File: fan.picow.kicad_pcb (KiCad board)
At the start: 2 copper layers, 73.4 x 70.5 mm, 64 parts, among them J1 12v Input, J12 DHT22, J2 Fan1, J3 Fan2, J4 Fan4, J5 Fan3, J7 OLED, Q1 AOD4184A, Q2 BSS138, SW1 EG1257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

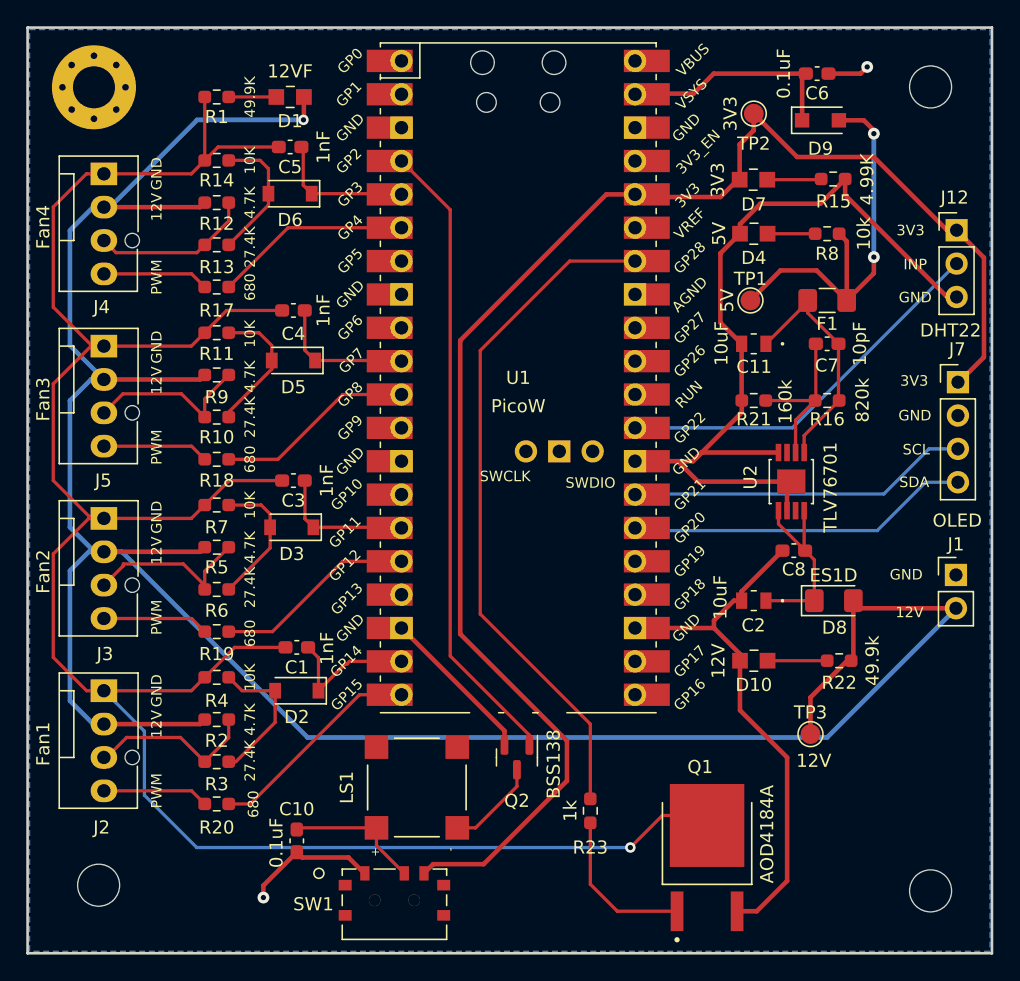
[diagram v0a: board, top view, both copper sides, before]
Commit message: cleanup all tracks and vias
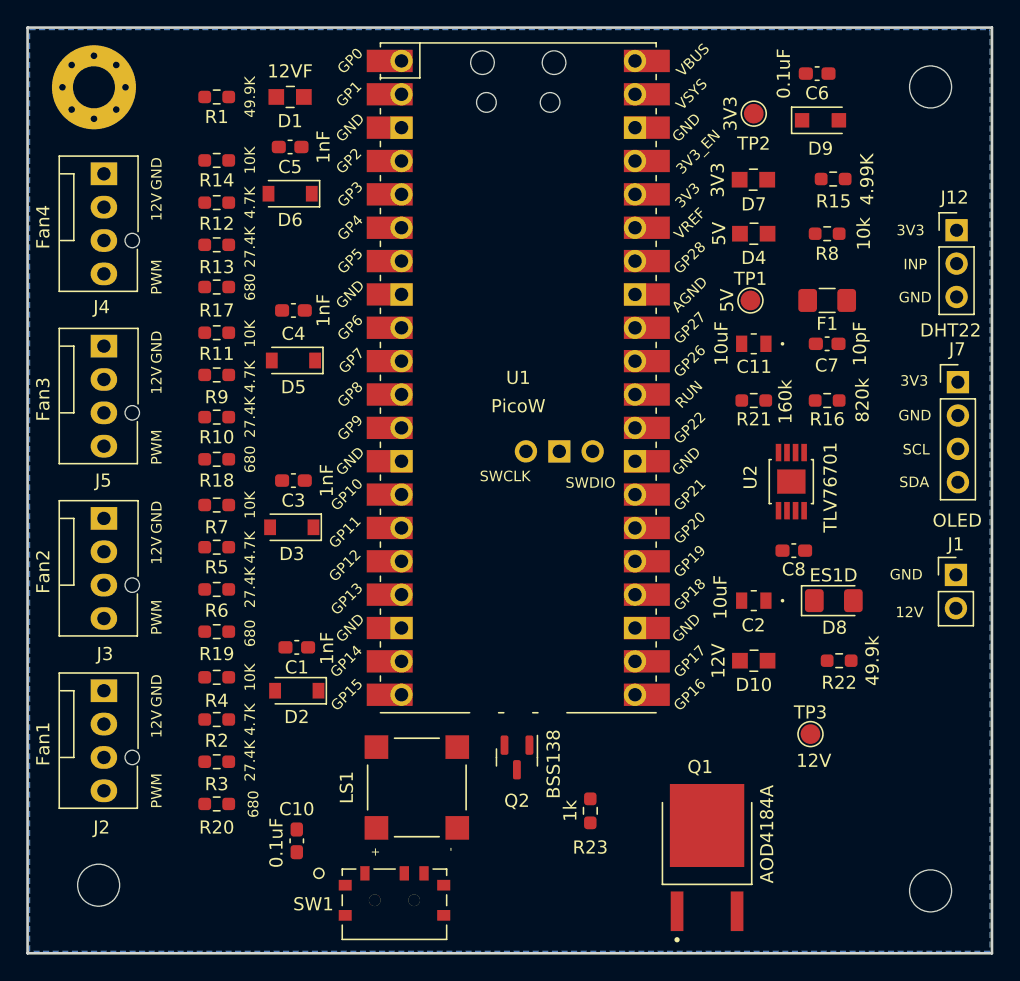
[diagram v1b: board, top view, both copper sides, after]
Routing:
- net /12V: track 194.0 -> 0.00 mm, vias 1 -> 0
- net /GNDFAN: track 171.3 -> 0.00 mm, vias 1 -> 0
- net GND: track 132.1 -> 0.00 mm, vias 2 -> 0
- net /3V3: track 115.1 -> 0.00 mm
- net /RELC: track 52.2 -> 0.00 mm
- net /BUZZ: track 48.5 -> 0.00 mm
- net /5V: track 31.3 -> 0.00 mm, vias 2 -> 0
- net /TEMPHUM: track 29.7 -> 0.00 mm
- net /SDA: track 26.2 -> 0.00 mm
- net /SCL: track 26.0 -> 0.00 mm
- net Net-(C11-Pad1): track 18.3 -> 0.00 mm
- net /VSYS: track 17.3 -> 0.00 mm
- net /PWM1: track 16.6 -> 0.00 mm
- net /PWM2: track 15.4 -> 0.00 mm
- net /PWM3: track 15.2 -> 0.00 mm
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
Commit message: first autorouting test
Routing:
- net /12V: track 0.00 -> 193.7 mm
- net /GNDFAN: track 0.00 -> 144.9 mm
- net /3V3: track 0.00 -> 112.2 mm, vias 0 -> 1
- net /BUZZ: track 0.00 -> 49.0 mm
- net /RELC: track 0.00 -> 43.9 mm
- net /SDA: track 0.00 -> 33.1 mm
- net /SCL: track 0.00 -> 30.6 mm
- net /TEMPHUM: track 0.00 -> 29.7 mm
- net GND: track 0.00 -> 25.0 mm, vias 0 -> 12
- net /5V: track 0.00 -> 22.3 mm
- net Net-(C11-Pad1): track 0.00 -> 17.8 mm
- net Net-(C2-Pad1): track 0.00 -> 16.9 mm
- net /VSYS: track 0.00 -> 16.7 mm
- net /PWM1: track 0.00 -> 16.6 mm
- net /PWM2: track 0.00 -> 15.4 mm
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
